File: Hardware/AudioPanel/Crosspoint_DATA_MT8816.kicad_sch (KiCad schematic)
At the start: 18 parts, among them SW6 ~{RESET}, U49 MCP23017_ML, U50 ICL7660, U51 MT8816AP1, U52 MT8816AP1

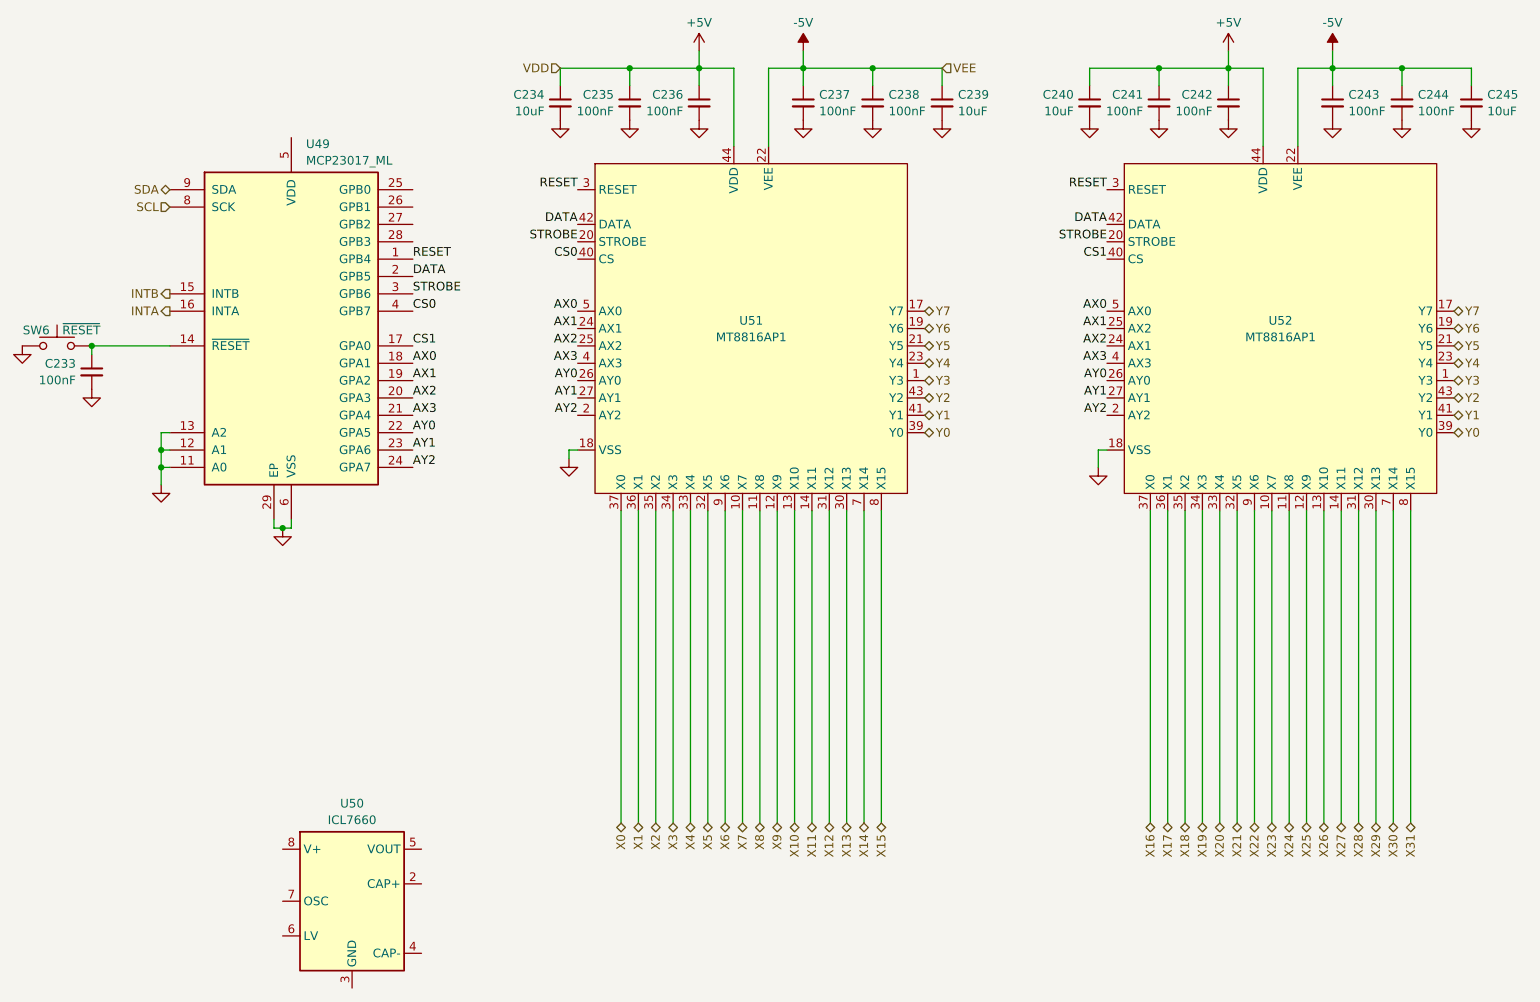
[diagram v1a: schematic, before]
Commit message: Realized that I need to rethink how I'm going to mix the radio audio with the stereo audio
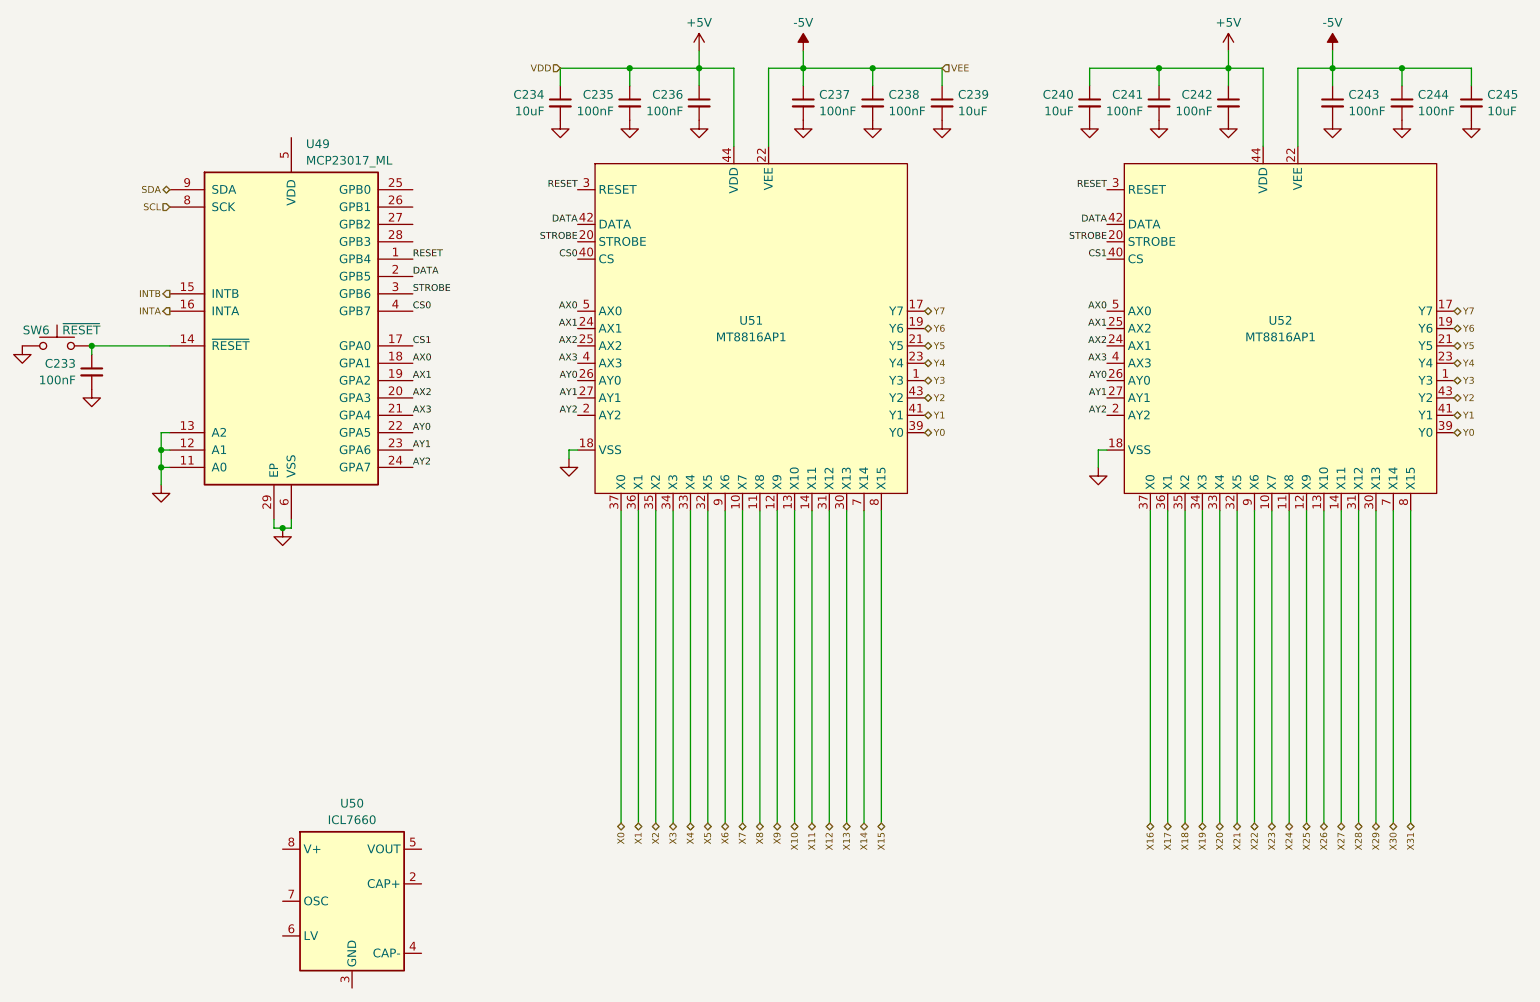
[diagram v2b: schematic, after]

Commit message: Cleaned up sheet voltage inputs
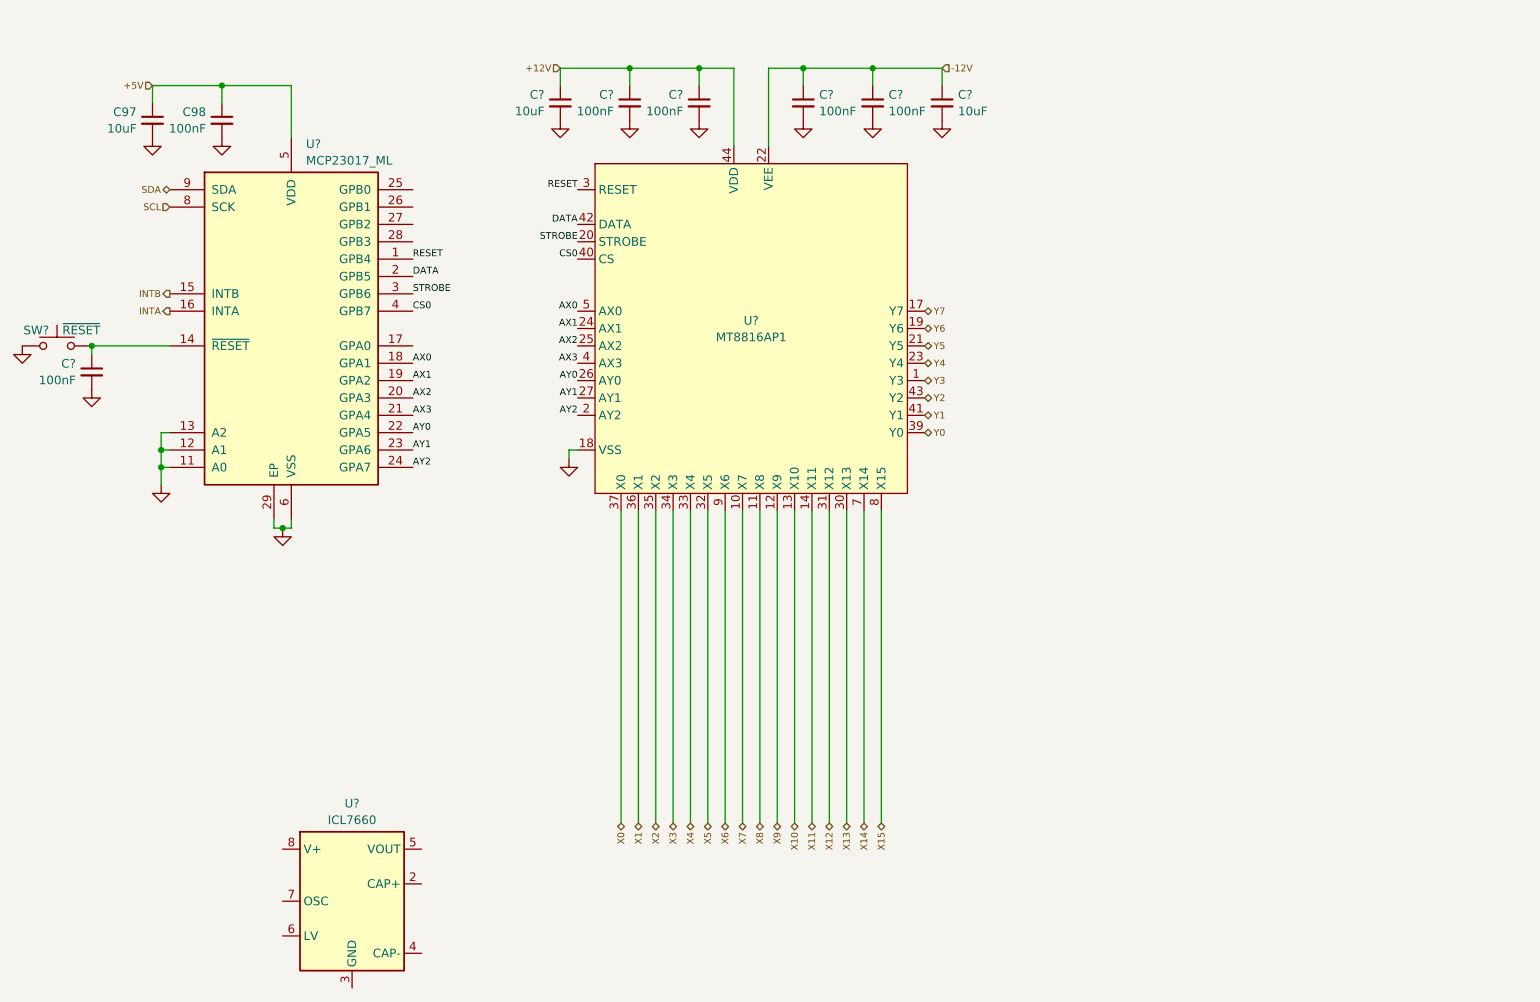
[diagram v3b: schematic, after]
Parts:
- removed C240, C245: 10uF, symbol Device:C_Small
- removed C241, C242, C243, C244: 100nF, symbol Device:C_Small
- removed U52: MT8816AP1, Package_LCC:PLCC-44, symbol AudioPanelLibrary:MT8816AP1
- added C97: 10uF, symbol Device:C_Small
- added C98: 100nF, symbol Device:C_Small
- renumbered C238 to C?, C236 to C?, C233 to C?, C235 to C?, C237 to C?, C234 to C?, C239 to C?, SW6 to SW?, U50 to U?, U51 to U?, U49 to U?
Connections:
- net +5V: now also U?.5 (VDD), C97.1, C98.1; no longer C?.1, C?.1, C?.1, U?.44 (VDD)
- net GND: now also C97.2, C98.2
- net -5V renamed -12V
- net CS1: no longer names the net of U?.17 (GPA0)
- new net +12V: C?.1, C?.1, C?.1, U?.44 (VDD)

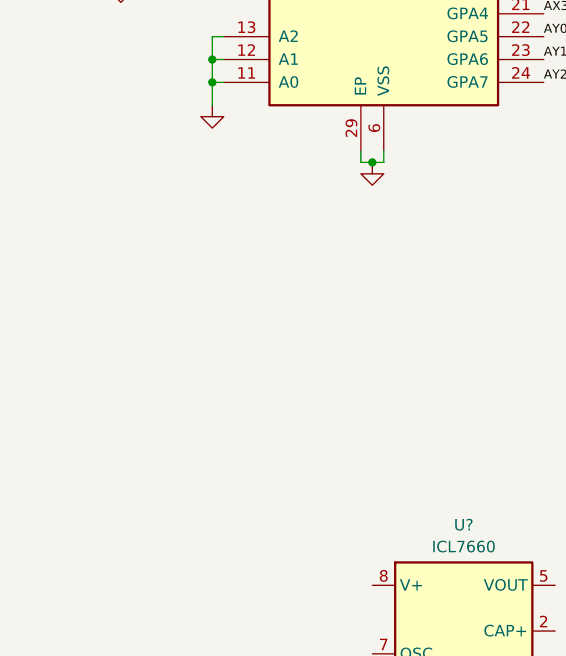
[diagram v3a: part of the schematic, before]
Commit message: Considering replacing some of the MCP23017s with 74HC594 shift register
Ken KC9UMR gave me this idea, would be cheaper option
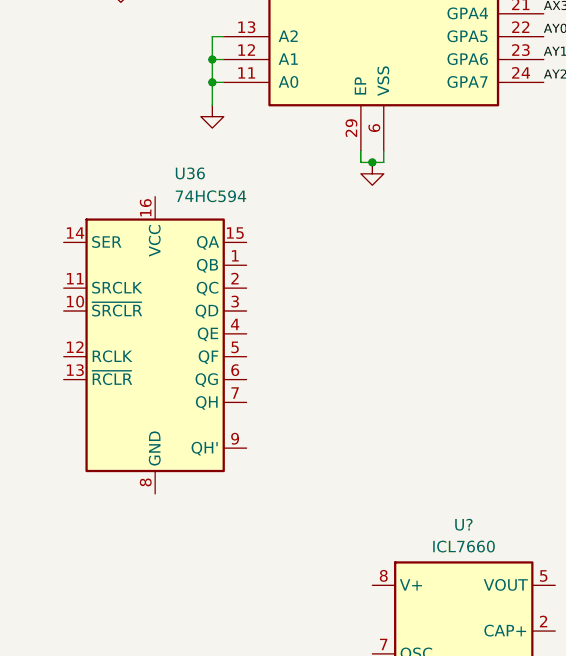
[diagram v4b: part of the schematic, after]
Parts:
- added U36: 74HC594, symbol 74xx:74HC594
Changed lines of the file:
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@@
+	)
+	(symbol
+		(lib_id "74xx:74HC594")
+		(at 48.26 116.84 0)
+		(unit 1)
+		(exclude_from_sim no)
+		(in_bom yes)
+		(on_board yes)
+		(dnp no)
+		(fields_autoplaced yes)
+		(property "Reference" "U36"
+			(at 50.4033 99.06 0)
+			(effects
+				(font
+					(size 1.27 1.27)
+				)
+				(justify left)
+			)
+		)
+		(property "Value" "74HC594"
+			(at 50.4033 101.6 0)
+			(effects
+				(font
+					(size 1.27 1.27)
+				)
+				(justify left)
+			)
+		)
+		(property "Footprint" ""
+			(at 48.26 116.84 0)
+			(effects
+				(font
+					(size 1.27 1.27)
+				)
+				(hide yes)
+			)
+		)
+		(property "Datasheet" "https://www.ti.com/lit/ds/symlink/sn74hc594.pdf"
+			(at 48.26 116.84 0)
+			(effects
+				(font
+					(size 1.27 1.27)
+				)
+				(hide yes)
+			)
+		)
+		(property "Description" "8-Bit Shift Registers With Output Registers"
+			(at 48.26 116.84 0)
+			(effects
+				(font
+					(size 1.27 1.27)
+				)
+				(hide yes)
+			)
+		)
+		(pin "14"
+		)
+		(pin "11"
+		)
+		(pin "10"
+		)
+		(pin "13"
+		)
+		(pin "8"
+		)
+		(pin "15"
+		)
+		(pin "12"
+		)
+		(pin "1"
+		)
+		(pin "16"
+		)
+		(pin "2"
+		)
+		(pin "9"
+		)
+		(pin "5"
+		)
+		(pin "4"
+		)
+		(pin "3"
+		)
+		(pin "7"
+		)
+		(pin "6"
+		)
+		(instances
+			(project ""
+				(path "/2de36a1b-eee5-458c-8325-256a7162eff5/c1ee6588-ede0-4856-ae1d-36ded9da6bf7/d2a58e22-e7e1-483f-9e51-68715d06e8bc"
+					(reference "U36")
+					(unit 1)
+				)
+			)
+		)
 	)
 	(symbol
